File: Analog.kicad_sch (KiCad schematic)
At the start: 20 parts, among them U3 74HC4051, U4 74HC4051, U5 OPA350

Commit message: production files
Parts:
- C12, C13, C15: value 0.1u -> 100n
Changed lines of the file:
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@@
     (pin "2")
     (instances
-      (project "travaulta rgb"
+      (project "travaulta"
         (path "/690df46b-b605-4617-b545-6aaced86d0fc/197f4772-e814-41eb-a239-e401e14c7029"
           (reference "C14") (unit 1)
@@
     (pin "2")
     (instances
-      (project "travaulta rgb"
+      (project "travaulta"
         (path "/690df46b-b605-4617-b545-6aaced86d0fc/197f4772-e814-41eb-a239-e401e14c7029"
           (reference "R20") (unit 1)
@@
     (pin "1")
     (instances
-      (project "travaulta rgb"
+      (project "travaulta"
         (path "/690df46b-b605-4617-b545-6aaced86d0fc/197f4772-e814-41eb-a239-e401e14c7029"
           (reference "#PWR0138") (unit 1)
@@
   (symbol (lib_id "Device:C_Small") (at 252.73 62.865 90) (unit 1)
     (in_bom yes) (on_board yes) (dnp no) (fields_autoplaced)
-    (property "Reference" "C15" (at 252.7363 55.88 90)
-      (effects (font (size 1.27 1.27)))
-    )
-    (property "Value" "0.1u" (at 252.7363 58.42 90)
+    (property "Reference" "C15" (at 252.7363 57.15 90)
+      (effects (font (size 1.27 1.27)))
+    )
+    (property "Value" "100n" (at 252.7363 59.69 90)
       (effects (font (size 1.27 1.27)))
     )
@@
     (pin "2")
     (instances
-      (project "travaulta rgb"
+      (project "travaulta"
         (path "/690df46b-b605-4617-b545-6aaced86d0fc/197f4772-e814-41eb-a239-e401e14c7029"
           (reference "C15") (unit 1)
@@
     (pin "7")
     (instances
-      (project "travaulta rgb"
+      (project "travaulta"
         (path "/690df46b-b605-4617-b545-6aaced86d0fc/197f4772-e814-41eb-a239-e401e14c7029"
           (reference "U5") (unit 1)
@@
     (pin "1")
     (instances
-      (project "travaulta rgb"
+      (project "travaulta"
         (path "/690df46b-b605-4617-b545-6aaced86d0fc/197f4772-e814-41eb-a239-e401e14c7029"
           (reference "#PWR0140") (unit 1)
@@
     (pin "9")
     (instances
-      (project "travaulta rgb"
+      (project "travaulta"
         (path "/690df46b-b605-4617-b545-6aaced86d0fc/197f4772-e814-41eb-a239-e401e14c7029"
           (reference "U3") (unit 1)
@@
     (pin "1")
     (instances
-      (project "travaulta rgb"
+      (project "travaulta"
         (path "/690df46b-b605-4617-b545-6aaced86d0fc/197f4772-e814-41eb-a239-e401e14c7029"
           (reference "#PWR0141") (unit 1)
@@
   (symbol (lib_id "Device:C_Small") (at 132.08 84.455 90) (unit 1)
     (in_bom yes) (on_board yes) (dnp no) (fields_autoplaced)
-    (property "Reference" "C12" (at 132.0863 77.47 90)
-      (effects (font (size 1.27 1.27)))
-    )
-    (property "Value" "0.1u" (at 132.0863 80.01 90)
+    (property "Reference" "C12" (at 132.0863 78.74 90)
+      (effects (font (size 1.27 1.27)))
+    )
+    (property "Value" "100n" (at 132.0863 81.28 90)
       (effects (font (size 1.27 1.27)))
     )
@@
     (pin "2")
     (instances
-      (project "travaulta rgb"
+      (project "travaulta"
         (path "/690df46b-b605-4617-b545-6aaced86d0fc/197f4772-e814-41eb-a239-e401e14c7029"
           (reference "C12") (unit 1)
@@
     (pin "2")
     (instances
-      (project "travaulta rgb"
+      (project "travaulta"
         (path "/690df46b-b605-4617-b545-6aaced86d0fc/197f4772-e814-41eb-a239-e401e14c7029"
           (reference "R10") (unit 1)
@@
     (pin "2")
     (instances
-      (project "travaulta rgb"
+      (project "travaulta"
         (path "/690df46b-b605-4617-b545-6aaced86d0fc/197f4772-e814-41eb-a239-e401e14c7029"
           (reference "R15") (unit 1)
@@
     (pin "2")
     (instances
-      (project "travaulta rgb"
+      (project "travaulta"
         (path "/690df46b-b605-4617-b545-6aaced86d0fc/197f4772-e814-41eb-a239-e401e14c7029"
           (reference "R11") (unit 1)
@@
     (pin "2")
     (instances
-      (project "travaulta rgb"
+      (project "travaulta"
         (path "/690df46b-b605-4617-b545-6aaced86d0fc/197f4772-e814-41eb-a239-e401e14c7029"
           (reference "R14") (unit 1)
@@
     (pin "1")
     (instances
-      (project "travaulta rgb"
+      (project "travaulta"
         (path "/690df46b-b605-4617-b545-6aaced86d0fc/197f4772-e814-41eb-a239-e401e14c7029"
           (reference "#PWR0136") (unit 1)
@@
     (pin "1")
     (instances
-      (project "travaulta rgb"
+      (project "travaulta"
         (path "/690df46b-b605-4617-b545-6aaced86d0fc/197f4772-e814-41eb-a239-e401e14c7029"
           (reference "#PWR0143") (unit 1)
@@
     (pin "9")
     (instances
-      (project "travaulta rgb"
+      (project "travaulta"
         (path "/690df46b-b605-4617-b545-6aaced86d0fc/197f4772-e814-41eb-a239-e401e14c7029"
           (reference "U4") (unit 1)
@@
     (pin "2")
     (instances
-      (project "travaulta rgb"
+      (project "travaulta"
         (path "/690df46b-b605-4617-b545-6aaced86d0fc/197f4772-e814-41eb-a239-e401e14c7029"
           (reference "R23") (unit 1)
@@
     (pin "1")
     (instances
-      (project "travaulta rgb"
+      (project "travaulta"
         (path "/690df46b-b605-4617-b545-6aaced86d0fc/197f4772-e814-41eb-a239-e401e14c7029"
           (reference "#PWR0148") (unit 1)
@@
     (pin "1")
     (instances
-      (project "travaulta rgb"
+      (project "travaulta"
         (path "/690df46b-b605-4617-b545-6aaced86d0fc/197f4772-e814-41eb-a239-e401e14c7029"
           (reference "#PWR0139") (unit 1)
@@
       (effects (font (size 1.27 1.27)))
     )
-    (property "Value" "0.1u" (at 133.3563 31.115 90)
+    (property "Value" "100n" (at 133.3563 31.115 90)
       (effects (font (size 1.27 1.27)))
     )
@@
     (pin "2")
     (instances
-      (project "travaulta rgb"
+      (project "travaulta"
         (path "/690df46b-b605-4617-b545-6aaced86d0fc/197f4772-e814-41eb-a239-e401e14c7029"
           (reference "C13") (unit 1)
@@
     (pin "2")
     (instances
-      (project "travaulta rgb"
+      (project "travaulta"
         (path "/690df46b-b605-4617-b545-6aaced86d0fc/197f4772-e814-41eb-a239-e401e14c7029"
           (reference "R21") (unit 1)
@@
     (pin "2")
     (instances
-      (project "travaulta rgb"
+      (project "travaulta"
         (path "/690df46b-b605-4617-b545-6aaced86d0fc/197f4772-e814-41eb-a239-e401e14c7029"
           (reference "R16") (unit 1)
@@
     (pin "2")
     (instances
-      (project "travaulta rgb"
+      (project "travaulta"
         (path "/690df46b-b605-4617-b545-6aaced86d0fc/197f4772-e814-41eb-a239-e401e14c7029"
           (reference "R17") (unit 1)
@@
     (pin "2")
     (instances
-      (project "travaulta rgb"
+      (project "travaulta"
         (path "/690df46b-b605-4617-b545-6aaced86d0fc/197f4772-e814-41eb-a239-e401e14c7029"
           (reference "R12") (unit 1)
@@
     (pin "2")
     (instances
-      (project "travaulta rgb"
+      (project "travaulta"
         (path "/690df46b-b605-4617-b545-6aaced86d0fc/197f4772-e814-41eb-a239-e401e14c7029"
           (reference "JP1") (unit 1)
@@
     (pin "1")
     (instances
-      (project "travaulta rgb"
+      (project "travaulta"
         (path "/690df46b-b605-4617-b545-6aaced86d0fc/197f4772-e814-41eb-a239-e401e14c7029"
           (reference "#PWR0135") (unit 1)
@@
     (pin "1")
     (instances
-      (project "travaulta rgb"
+      (project "travaulta"
         (path "/690df46b-b605-4617-b545-6aaced86d0fc/197f4772-e814-41eb-a239-e401e14c7029"
           (reference "#PWR0134") (unit 1)
@@
     (pin "1")
     (instances
-      (project "travaulta rgb"
+      (project "travaulta"
         (path "/690df46b-b605-4617-b545-6aaced86d0fc/197f4772-e814-41eb-a239-e401e14c7029"
           (reference "#PWR0142") (unit 1)
@@
     (pin "2")
     (instances
-      (project "travaulta rgb"
+      (project "travaulta"
         (path "/690df46b-b605-4617-b545-6aaced86d0fc/197f4772-e814-41eb-a239-e401e14c7029"
           (reference "R19") (unit 1)
@@
     (pin "1")
     (instances
-      (project "travaulta rgb"
+      (project "travaulta"
         (path "/690df46b-b605-4617-b545-6aaced86d0fc/197f4772-e814-41eb-a239-e401e14c7029"
           (reference "#PWR0137") (unit 1)
@@
     (pin "2")
     (instances
-      (project "travaulta rgb"
+      (project "travaulta"
         (path "/690df46b-b605-4617-b545-6aaced86d0fc/197f4772-e814-41eb-a239-e401e14c7029"
           (reference "R13") (unit 1)

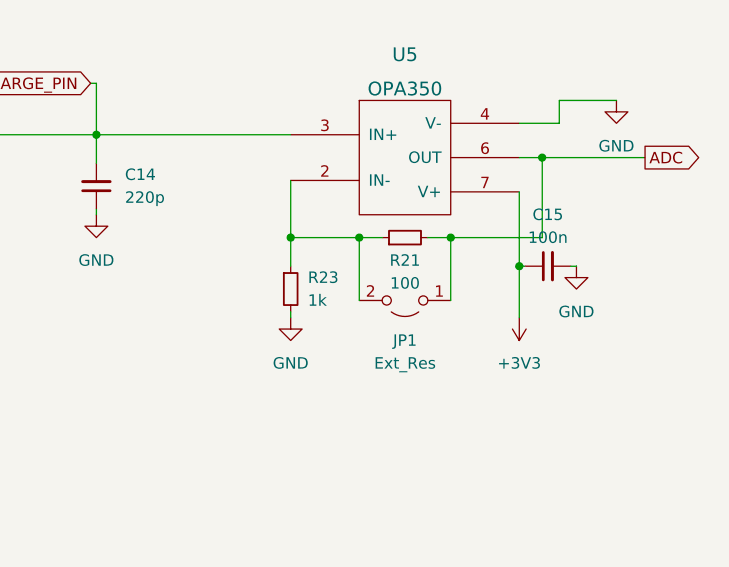
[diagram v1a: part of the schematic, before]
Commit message: MCU swap, UCB components moved, crystal swap
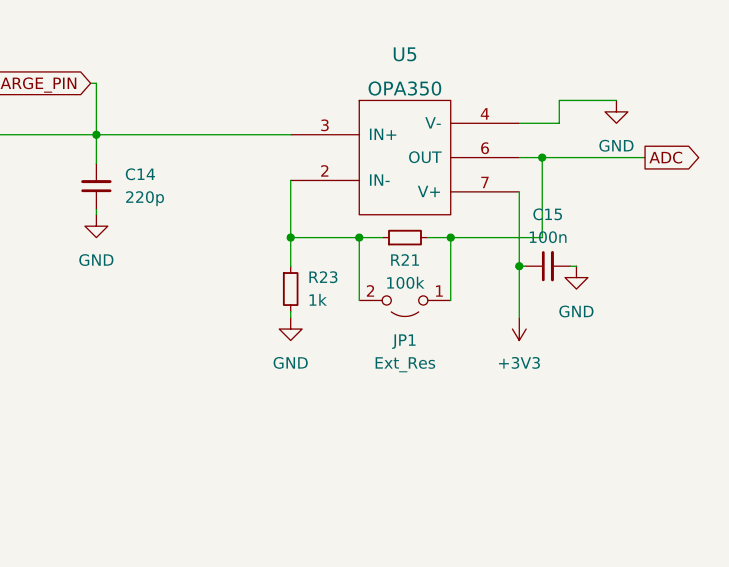
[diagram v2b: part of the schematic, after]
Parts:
- R21: value 100 -> 100k
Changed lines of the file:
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@@
       (effects (font (size 1.27 1.27)))
     )
-    (property "Value" "100" (at 236.855 64.77 90)
+    (property "Value" "100k" (at 236.855 64.77 90)
       (effects (font (size 1.27 1.27)))
     )

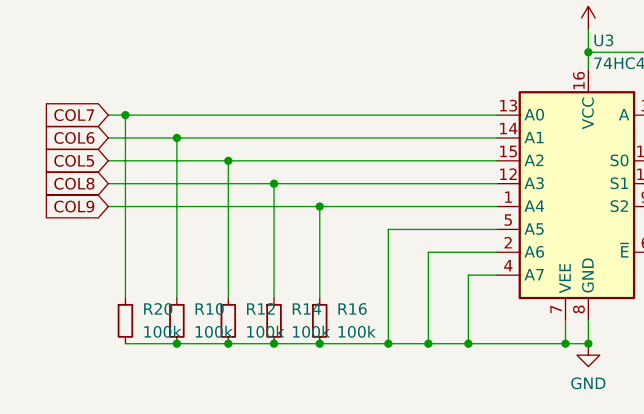
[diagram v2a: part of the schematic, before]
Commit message: one pin matrix fix
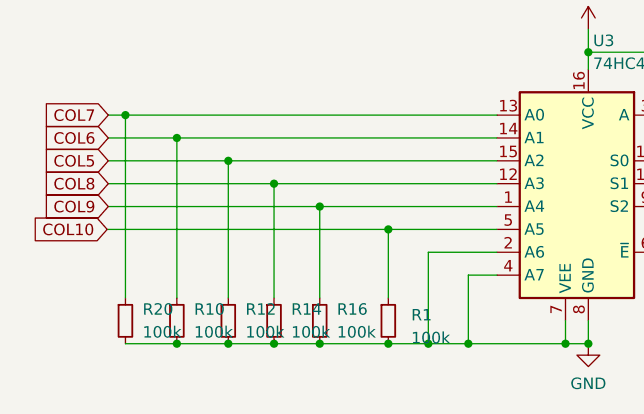
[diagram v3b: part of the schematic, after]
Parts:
- added R1: 100k, Resistor_SMD:R_0402_1005Metric, symbol Device:R_Small
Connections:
- net GND: now also R1.2; no longer U3.5 (A5)
- new net COL10: R1.1, U3.5 (A5)
